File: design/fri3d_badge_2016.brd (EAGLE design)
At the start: 80 x 70 mm, 40 parts, among them Q1 MOSFET-NCHANNEL2N7002PW, U1 MCP73831, Y1 8MHz

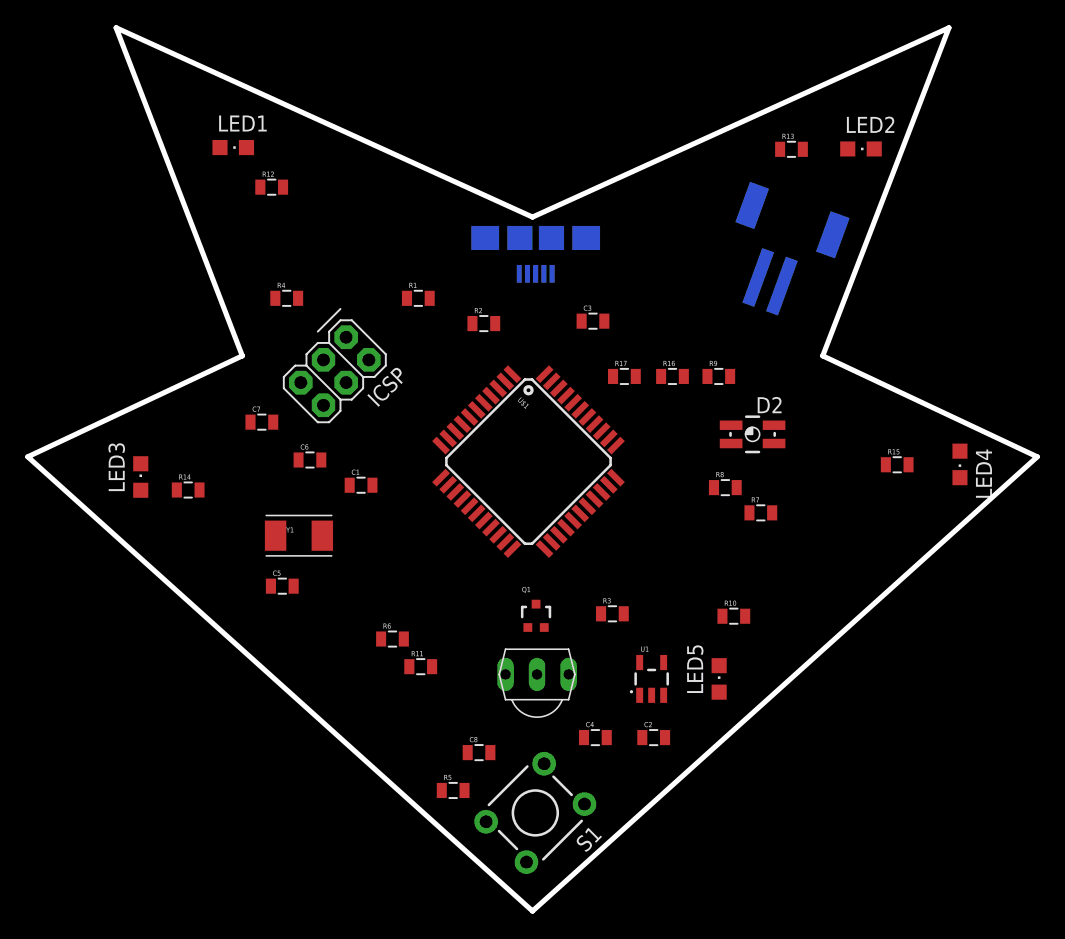
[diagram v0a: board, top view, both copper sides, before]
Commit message: created first version (draft) PCB layout
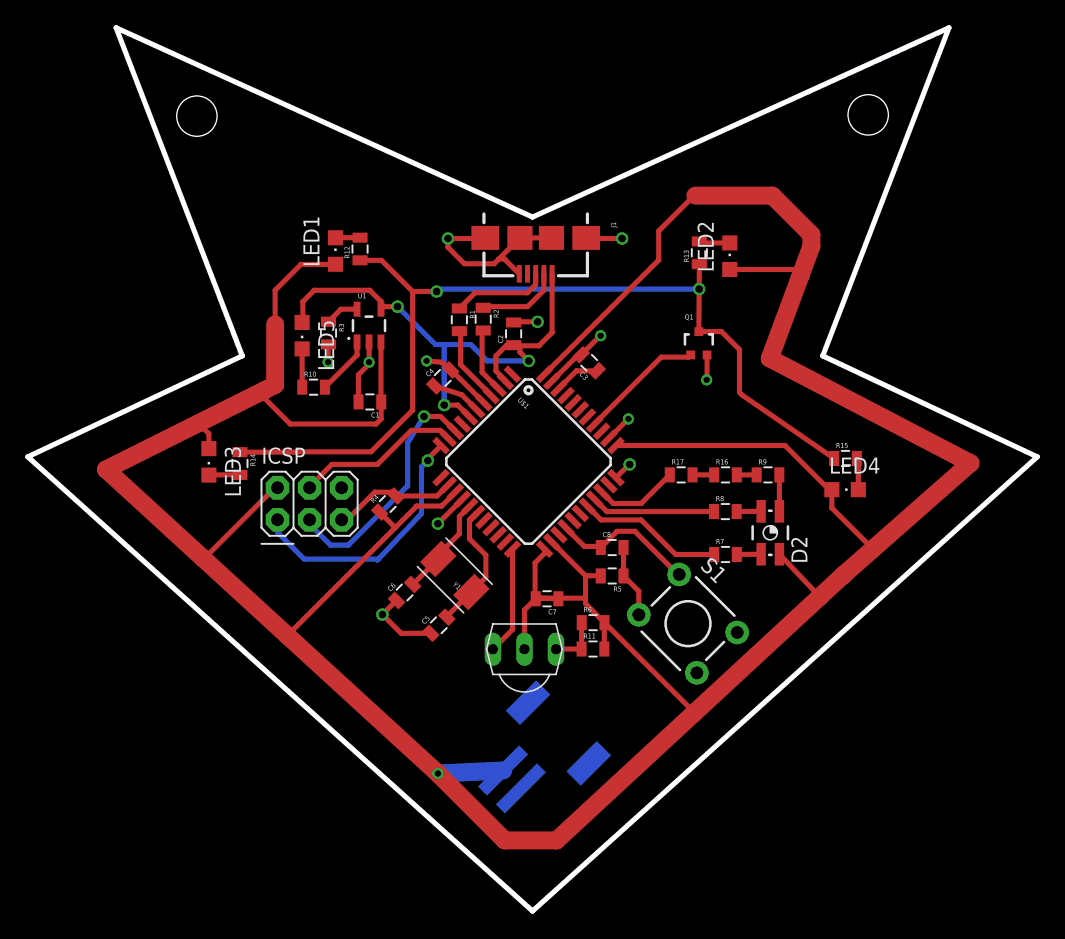
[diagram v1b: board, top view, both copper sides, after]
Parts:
- moved J2 44.6 mm to (41.0, 13.1), turned to 45 degrees
- moved LED5 42.8 mm to (21.7, 45.6), turned to 180 degrees
- moved R10 37.9 mm to (22.6, 41.5)
- moved U1 35.9 mm to (27.0, 46.4)
- moved C2 33.9 mm to (38.5, 45.8), turned to 90 degrees
- moved R3 31.6 mm to (23.8, 45.8), turned to 270 degrees
- moved C4 31.0 mm to (32.9, 42.2), turned to 45 degrees
- moved C7 26.6 mm to (41.1, 24.8), turned to 180 degrees
- moved Q1 25.2 mm to (53.2, 45.0)
- moved R5 21.2 mm to (46.3, 26.6), turned to 180 degrees
- moved C8 19.4 mm to (46.3, 28.8)
- moved S1 19.3 mm to (52.3, 22.8), turned to 315 degrees
- moved R4 18.2 mm to (28.5, 32.3), turned to 45 degrees
- moved R6 16.0 mm to (44.8, 22.9)
- moved R11 13.7 mm to (44.8, 20.8)
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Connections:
- net BUTTON: now also U$1.26; no longer U$1.1
- net IR_RX: now also U$1.22; no longer U$1.32
- net IR_TX: now also U$1.37; no longer U$1.31
- net N$13: now also LED1.C; no longer LED1.A
- net N$14: now also LED2.C; no longer LED2.A
- net N$15: now also LED3.C; no longer LED3.A
- net N$16: now also LED4.C; no longer LED4.A
- net RGB_RED: now also U$1.31; no longer U$1.12
- net VCC: now also LED1.A, LED2.A, LED3.A, LED4.A; no longer LED1.C, LED2.C, LED3.C, LED4.C
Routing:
- net VCC: track 0.00 -> 293.6 mm, vias 0 -> 1
- net N$24: track 0.00 -> 74.2 mm, vias 0 -> 2
- net GND: track 0.00 -> 61.7 mm, vias 0 -> 12
- net USBVCC: track 0.00 -> 43.7 mm, vias 0 -> 3
- net MISO: track 0.00 -> 21.0 mm, vias 0 -> 1
- net SCK: track 0.00 -> 19.6 mm, vias 0 -> 1
- net MOSI: track 0.00 -> 13.2 mm
- net RGB_BLUE: track 0.00 -> 11.6 mm
- net BUTTON: track 0.00 -> 11.6 mm
- net N$8: track 0.00 -> 10.3 mm
- net IR_TX: track 0.00 -> 9.90 mm
- net RGB_GREEN: track 0.00 -> 9.88 mm
- net RST: track 0.00 -> 9.85 mm
- net IR_RX: track 0.00 -> 8.58 mm
- net N$9: track 0.00 -> 8.11 mm
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- added copper zone on layer 16, net GND
- added copper zone on layer 16, net N$18

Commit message: layout tweaks -> v2
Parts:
- removed J1: (no value), SparkFun-Connectors:USB-AB-MICRO-SMD
- removed J2: (no value), SparkFun-Connectors:JST-2-SMD
- removed Y1: 8MHz, SparkFun-FreqCtrl:CRYSTAL-TXC-7A
- added J3: (no value), SparkFun-Connectors:JST-2-PTH-VERT
- added K1: 65100516121, Input-Output_Connectors_rev15d:65100516121
- added Q2: (no value), crystal:HC49/S
- moved C2 8.20 mm to (30.5, 44.0)
- moved U$3 4.69 mm to (40.3, 16.2)
- moved C5 3.85 mm to (30.8, 19.2)
- moved C6 3.75 mm to (27.3, 22.6)
- moved C7 2.10 mm to (43.2, 24.9)
- moved R1 1.63 mm to (35.4, 48.0), turned to 180 degrees
- moved R2 1.25 mm to (35.5, 45.8), turned to 180 degrees
- moved C4 0.52 mm to (32.4, 42.1), turned to 90 degrees
- moved R5 0.10 mm to (46.3, 26.7)
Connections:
- net GND: now also J3.1, K1.5, K1.Z1, K1.Z2, K1.Z3, K1.Z4; no longer J1.GND, J1.SHIELD1, J1.SHIELD2, J1.SHIELD3, J1.SHIELD4, J2.1
- net N$1: now also K1.2; no longer J1.D-
- net N$2: now also K1.3; no longer J1.D+
- net N$8: now also Q2.2; no longer Y1.P$2
- net N$9: now also Q2.1; no longer Y1.P$1
- net USBVCC: now also K1.1; no longer J1.VBUS
- net VCC: now also J3.2; no longer J2.2
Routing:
- net GND: track 61.7 -> 51.2 mm, vias 12 -> 9
- net VCC: track 293.6 -> 283.5 mm, vias 1 -> 0
- net N$9: track 8.11 -> 12.5 mm
- net IR_RX: track 8.58 -> 12.8 mm
- net N$24: track 74.2 -> 78.1 mm
- net N$8: track 10.3 -> 13.7 mm
- net N$10: track 4.13 -> 7.32 mm
- net D+: track 6.15 -> 8.91 mm
- net N$2: track 7.68 -> 9.54 mm, vias 0 -> 1
- net USBVCC: track 43.7 -> 41.9 mm
- net SCK: track 19.6 -> 20.2 mm
- net D-: track 5.16 -> 5.66 mm
- net N$1: track 6.69 -> 6.91 mm, vias 0 -> 1
- removed copper zone on layer 16, net N$18

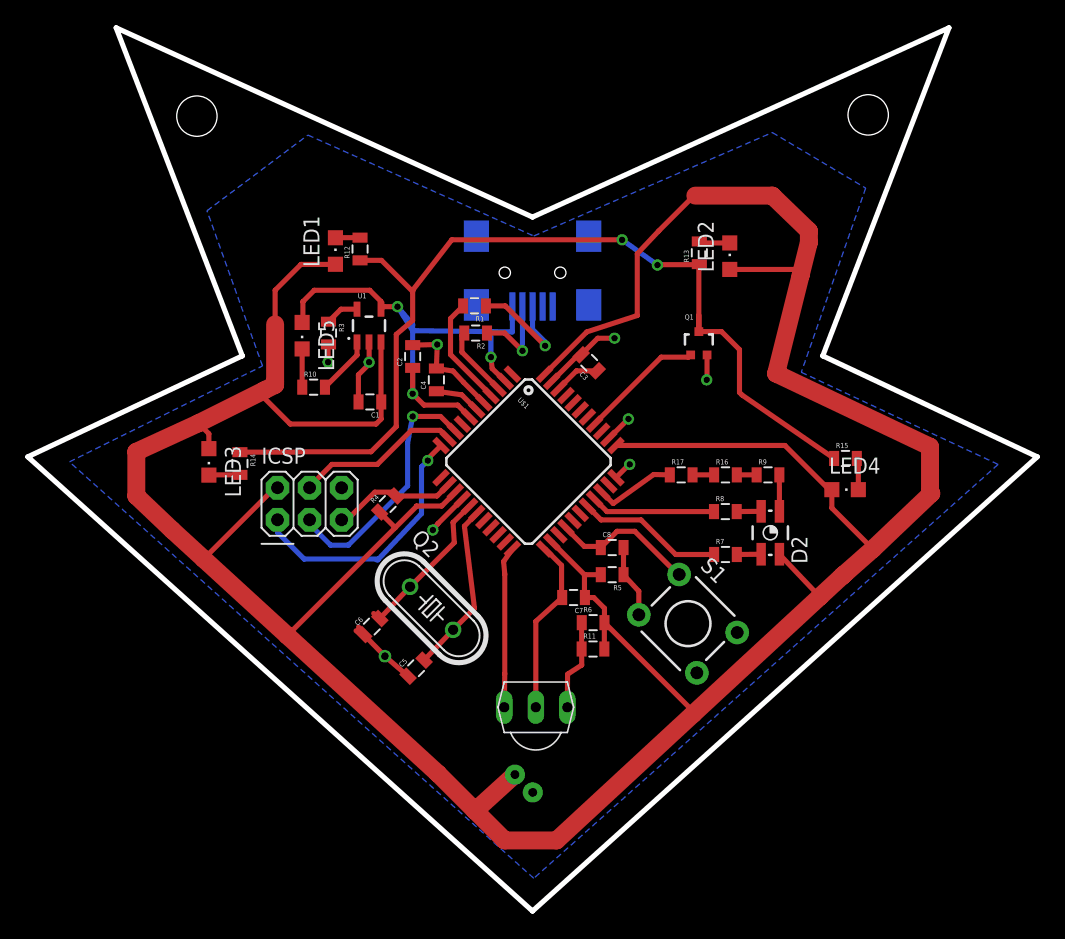
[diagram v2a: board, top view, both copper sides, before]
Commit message: fixed wrongly connected IR LED net
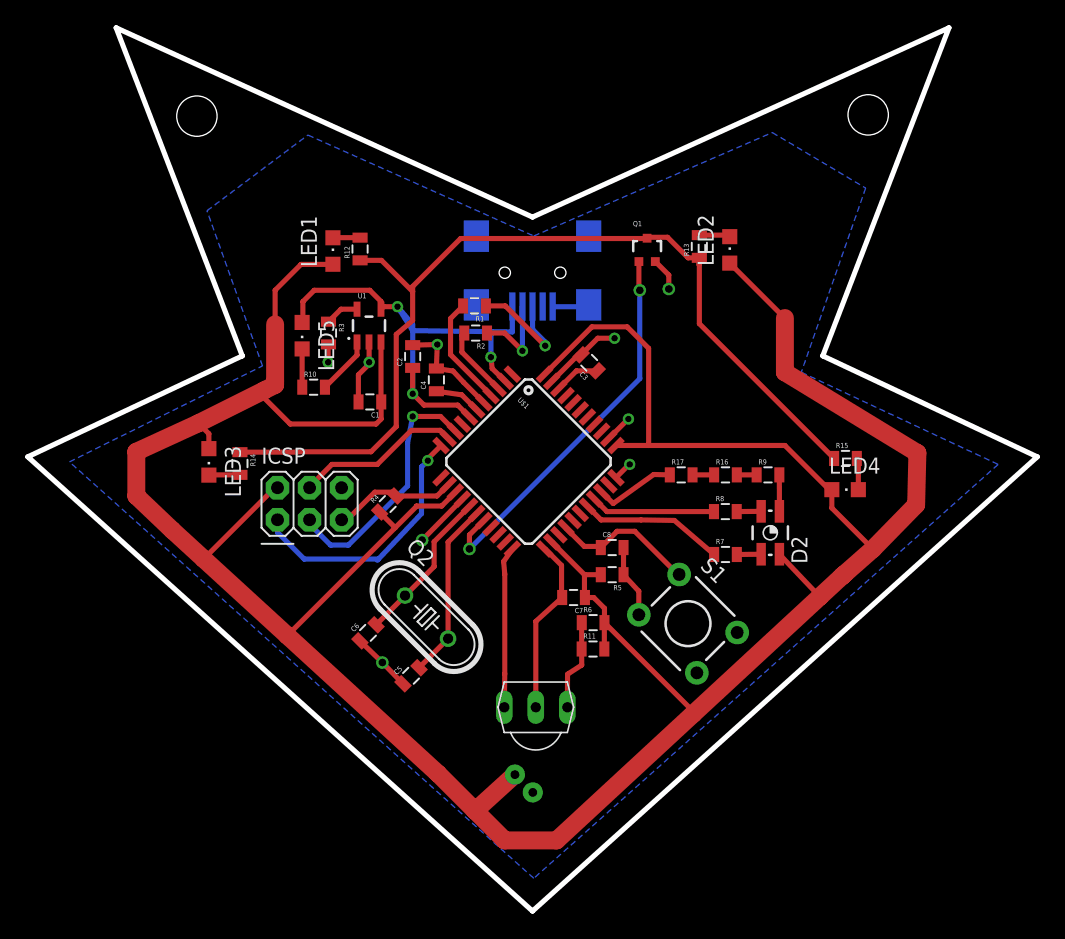
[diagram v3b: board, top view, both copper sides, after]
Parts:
- moved Q1 8.46 mm to (49.1, 52.4)
- moved Q2 0.81 mm to (31.6, 23.3)
- moved C5 0.72 mm to (30.4, 18.6)
- moved C6 0.58 mm to (27.0, 22.1)
- moved LED2 0.50 mm to (55.6, 52.4)
- moved R13 0.50 mm to (53.2, 52.7)
- moved LED1 0.20 mm to (24.2, 52.3)
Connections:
- net IR_TX: now also U$1.18; no longer U$1.37
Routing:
- net VCC: track 283.5 -> 261.7 mm
- net IR_TX: track 9.90 -> 31.1 mm, vias 0 -> 2
- net GND: track 51.2 -> 54.5 mm
- net N$24: track 78.1 -> 76.0 mm, vias 2 -> 0
